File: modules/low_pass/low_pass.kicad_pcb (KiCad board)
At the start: 2 copper layers, 30.5 x 68.6 mm, 31 parts, among them U1 MCP6002-xSN, U2 VTL5C, U3 MCP6002-xSN, U4 MCP6002-xSN, U5 VTL5C, U6 VTL5C

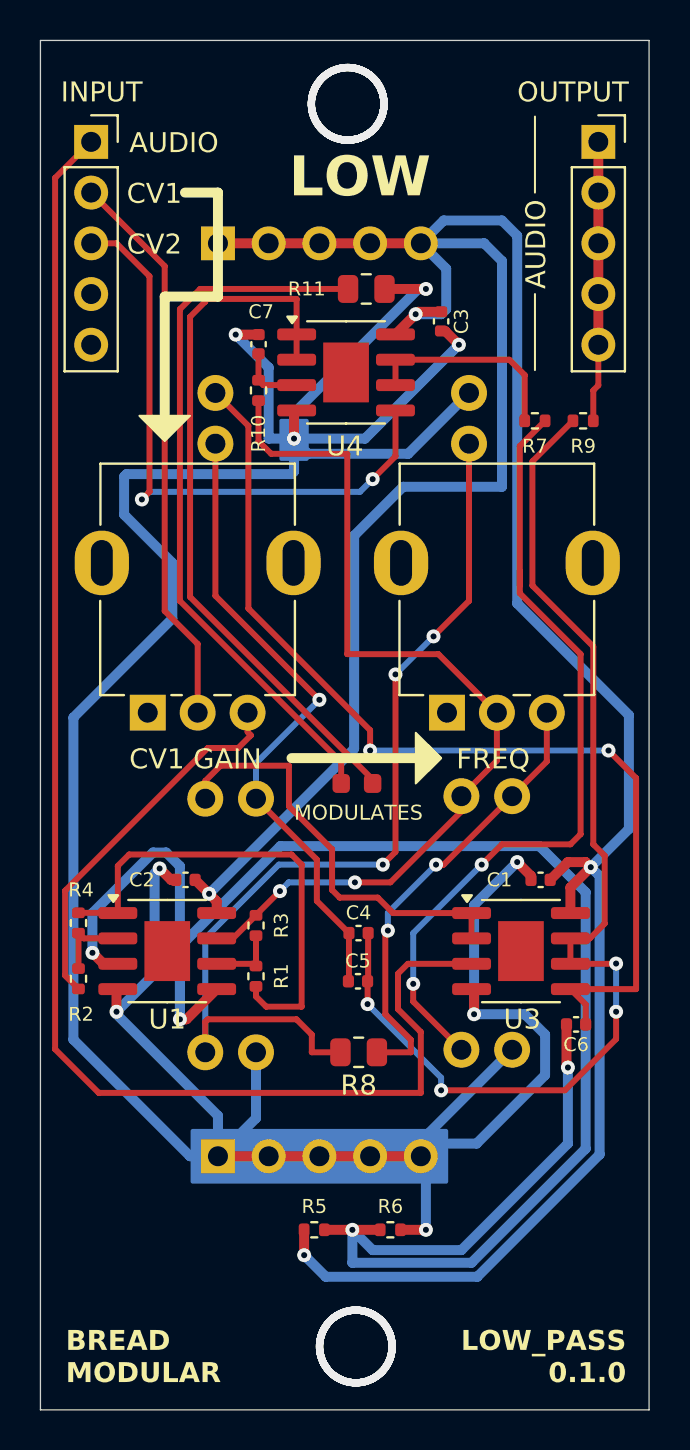
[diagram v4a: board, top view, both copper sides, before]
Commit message: Introduced new low_pass gate.
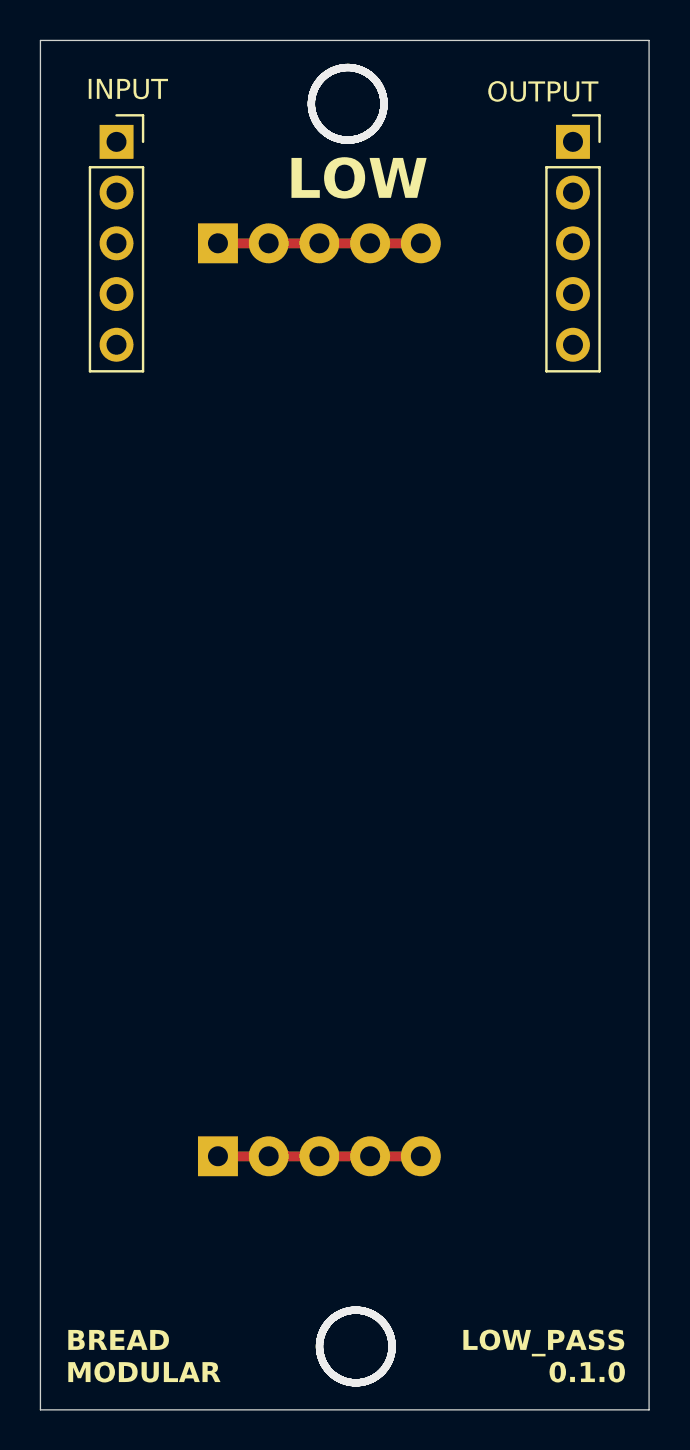
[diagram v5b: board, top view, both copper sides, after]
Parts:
- removed 5V1: Conn_01x05_Pin, Connector_PinHeader_2.54mm:PinHeader_1x05_P2.54mm_Vertical
- removed C1, C2, C3, C7: 0.1uf, Capacitor_SMD:C_0402_1005Metric
- removed C4, C5, C6: 1nf, Capacitor_SMD:C_0402_1005Metric
- removed D1: LED, LED_SMD:LED_0603_1608Metric
- removed R1, R10, R2, R3, R7: 100k, Resistor_SMD:R_0402_1005Metric
- removed R11, R8: 330, Resistor_SMD:R_0805_2012Metric
- removed R4: 200k, Resistor_SMD:R_0402_1005Metric
- removed R5, R6, R9: 1k, Resistor_SMD:R_0402_1005Metric
- removed RV1, RV2: 1M, BreadModular_Pots:Potentiometer_RV09
- removed U1, U3, U4: MCP6002-xSN, Package_SO:SOIC-8-1EP_3.9x4.9mm_P1.27mm_EP2.29x3mm
- removed U2, U5, U6: VTL5C, BreadModular_MISC:VTL5C
- added V_SUPPLY1: Conn_01x05_Pin, BreadModular_MISC:Power_Connector, B.Cu at (55.9, 50.8)
- GND1: footprint Connector_PinHeader_2.54mm:PinHeader_1x05_P2.54mm_Vertical -> BreadModular_MISC:Power_Connector
- moved OUTPUT1 1.27 mm to (73.7, 45.7)
- moved INPUT1 1.27 mm to (50.8, 45.7)
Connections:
- INPUT1 pad 1: AUDIO_IN -> unconnected-(INPUT1-Pin_1-Pad1)
- INPUT1 pad 2: MOD_CV_IN -> unconnected-(INPUT1-Pin_2-Pad2)
- INPUT1 pad 3: CUTOFF_CV_IN -> unconnected-(INPUT1-Pin_3-Pad3)
- OUTPUT1 pad 1: AUDIO_OUT -> unconnected-(OUTPUT1-Pin_1-Pad1)
- OUTPUT1 pad 2: AUDIO_OUT -> unconnected-(OUTPUT1-Pin_2-Pad2)
- OUTPUT1 pad 3: AUDIO_OUT -> unconnected-(OUTPUT1-Pin_3-Pad3)
- OUTPUT1 pad 4: AUDIO_OUT -> unconnected-(OUTPUT1-Pin_4-Pad4)
- OUTPUT1 pad 5: AUDIO_OUT -> unconnected-(OUTPUT1-Pin_5-Pad5)
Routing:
- net GND: track 168.1 -> 10.2 mm, vias 9 -> 0
- net +5V: track 144.8 -> 0.00 mm, vias 4 -> 0
- net +2.5V: track 97.3 -> 0.00 mm, vias 4 -> 0
- net AUDIO_IN: track 75.7 -> 0.00 mm
- net Net-(U3B--): track 56.1 -> 0.00 mm, vias 4 -> 0
- net Net-(U3B-+): track 51.5 -> 0.00 mm, vias 2 -> 0
- net Net-(U5-+): track 48.5 -> 0.00 mm, vias 3 -> 0
- net PROCESSED_MOD_CV: track 46.1 -> 0.00 mm, vias 2 -> 0
- net Net-(U2-+): track 40.5 -> 0.00 mm, vias 2 -> 0
- net Net-(D1-A): track 36.0 -> 0.00 mm
- net Net-(D1-K): track 35.9 -> 0.00 mm
- net Net-(C4-Pad1): track 32.3 -> 0.00 mm, vias 1 -> 0
- net CUTOFF_CV_IN: track 30.8 -> 0.00 mm, vias 2 -> 0
- net MOD_CV_IN: track 28.3 -> 0.00 mm
- net Net-(R1-Pad1): track 24.1 -> 0.00 mm
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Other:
- board text removed: "AUDIO"
- board text removed: "CV1"
- board text removed: "CV1 GAIN"
- board text removed: "CV2"
- board text removed: "FREQ"
- board text removed: "MODULATES"

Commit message: Finalized the schematic of low_pass
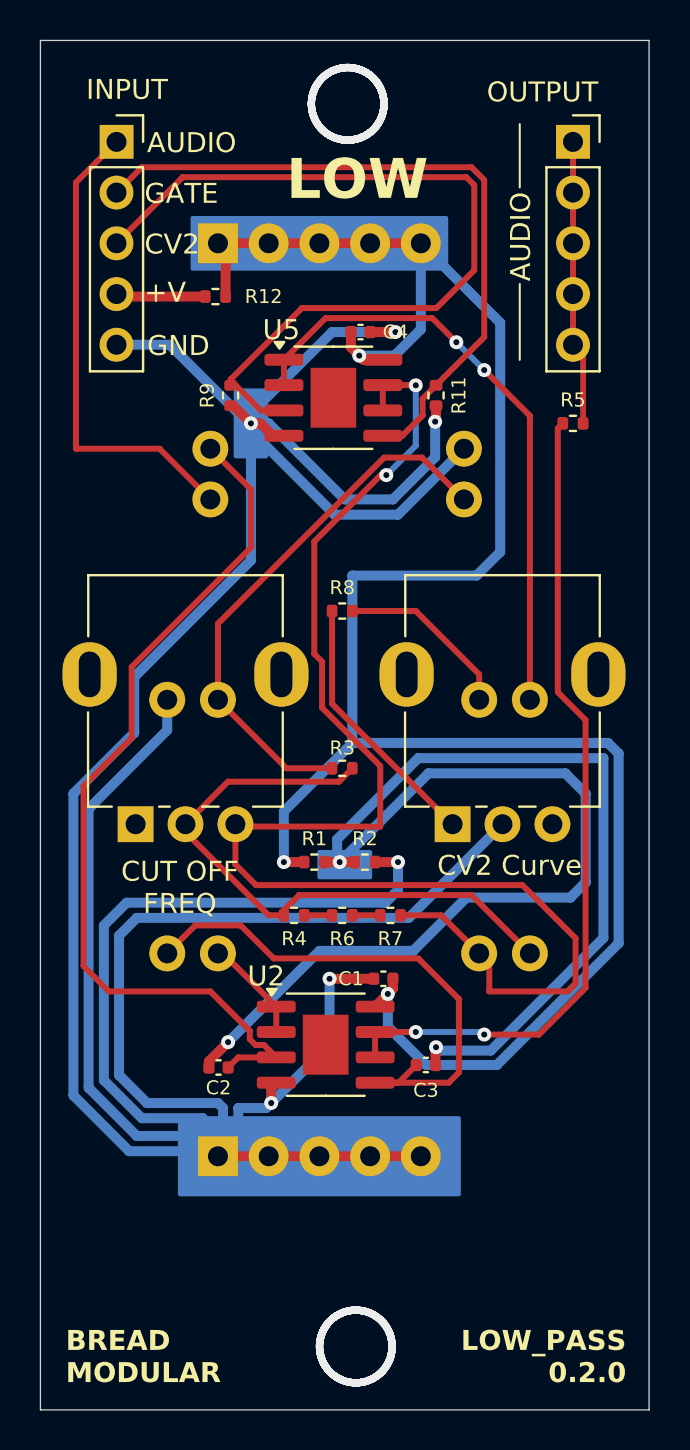
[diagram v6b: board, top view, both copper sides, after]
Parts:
- added C1: 0.1uf, Capacitor_SMD:C_0402_1005Metric, F.Cu at (64.2, 87.6)
- added C2: 10nf, Capacitor_SMD:C_0402_1005Metric, F.Cu at (55.9, 92.1)
- added C3: 10nf, Capacitor_SMD:C_0402_1005Metric, F.Cu at (66.3, 91.9)
- added C4: 0.1uf, Capacitor_SMD:C_0402_1005Metric, F.Cu at (63.0, 55.2)
- added R1: 1k, Resistor_SMD:R_0402_1005Metric, F.Cu at (60.7, 81.8)
- added R11: 1M, Resistor_SMD:R_0402_1005Metric, F.Cu at (66.8, 58.4)
- added R12: 10k, Resistor_SMD:R_0402_1005Metric, F.Cu at (55.8, 53.5)
- added R2: 1k, Resistor_SMD:R_0402_1005Metric, F.Cu at (63.2, 81.8)
- added R3: 560, Resistor_SMD:R_0402_1005Metric, F.Cu at (62.1, 77.1)
- added R4: 200k, Resistor_SMD:R_0402_1005Metric, F.Cu at (59.7, 84.5)
- added R5: 1k, Resistor_SMD:R_0402_1005Metric, F.Cu at (73.7, 59.8)
- added R6: 200k, Resistor_SMD:R_0402_1005Metric, F.Cu at (62.1, 84.5)
- added R7: 200k, Resistor_SMD:R_0402_1005Metric, F.Cu at (64.5, 84.5)
- added R8: 560, Resistor_SMD:R_0402_1005Metric, F.Cu at (62.1, 69.2)
- added R9: 1M, Resistor_SMD:R_0402_1005Metric, F.Cu at (56.5, 58.4)
- added RV1: 1M, BreadModular_Pots:Potentiometer_RV09, F.Cu at (51.8, 79.9)
- added RV2: 1M, BreadModular_Pots:Potentiometer_RV09, F.Cu at (67.6, 79.9)
- added U1: VTL5C, BreadModular_MISC:VTL5C, B.Cu at (61.8, 62.4)
- added U2: MCP6002-xSN, Package_SO:SOIC-8-1EP_3.9x4.9mm_P1.27mm_EP2.29x3mm, F.Cu at (61.3, 90.9)
- added U3: VTL5C, BreadModular_MISC:VTL5C, B.Cu at (54.6, 80.0)
- added U4: VTL5C, BreadModular_MISC:VTL5C, B.Cu at (70.2, 80.0)
- added U5: MCP6002-xSN, Package_SO:SOIC-8-1EP_3.9x4.9mm_P1.27mm_EP2.29x3mm, F.Cu at (61.7, 58.5)
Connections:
- INPUT1 pad 1: unconnected-(INPUT1-Pin_1-Pad1) -> AUDIO_IN
- INPUT1 pad 2: unconnected-(INPUT1-Pin_2-Pad2) -> GATE_CV
- INPUT1 pad 3: unconnected-(INPUT1-Pin_3-Pad3) -> CUT_OFF_CV
- INPUT1 pad 4: unconnected-(INPUT1-Pin_4-Pad4) -> Net-(INPUT1-Pin_4)
- INPUT1 pad 5: unconnected-(INPUT1-Pin_5-Pad5) -> GND
- OUTPUT1 pad 1: unconnected-(OUTPUT1-Pin_1-Pad1) -> AUDIO_OUT
- OUTPUT1 pad 2: unconnected-(OUTPUT1-Pin_2-Pad2) -> AUDIO_OUT
- OUTPUT1 pad 3: unconnected-(OUTPUT1-Pin_3-Pad3) -> AUDIO_OUT
- OUTPUT1 pad 4: unconnected-(OUTPUT1-Pin_4-Pad4) -> AUDIO_OUT
- OUTPUT1 pad 5: unconnected-(OUTPUT1-Pin_5-Pad5) -> AUDIO_OUT
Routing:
- net GND: track 10.2 -> 221.7 mm, vias 0 -> 6
- net V_SUPPLY: track 10.2 -> 106.7 mm, vias 0 -> 3
- net V_MID: track 0.00 -> 80.3 mm, vias 0 -> 3
- net Net-(U5B--): track 0.00 -> 70.1 mm, vias 0 -> 2
- net Net-(U2A-+): track 0.00 -> 44.6 mm
- net Net-(U2B--): track 0.00 -> 41.8 mm, vias 0 -> 2
- net CUT_OFF_CV: track 0.00 -> 41.7 mm
- net GATE_CV: track 0.00 -> 34.7 mm
- net Net-(U4-+): track 0.00 -> 30.7 mm, vias 0 -> 2
- net Net-(R3-Pad2): track 0.00 -> 30.7 mm
- net Net-(U1-+): track 0.00 -> 27.6 mm
- net Net-(U2B-+): track 0.00 -> 27.2 mm
- net AUDIO_IN: track 0.00 -> 24.0 mm
- net AUDIO_OUT: track 0.00 -> 14.3 mm
- net Net-(R8-Pad1): track 0.00 -> 13.2 mm
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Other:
- board text added: "+V"
- board text added: "AUDIO"
- board text added: "CUT OFF FREQ"
- board text added: "CV2"
- board text added: "CV2 Curve"
- board text added: "GATE"
- board text added: "GND"
- board text added: "LOW_PASS 0.2.0"
- board text removed: "LOW_PASS 0.1.0"
